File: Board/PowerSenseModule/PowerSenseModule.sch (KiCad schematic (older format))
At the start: 28 parts, among them J1 Conn_01x06_Male, U1 TPS82150

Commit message: Generated gerber and fab files
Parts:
- added G1: LOGO, Logo:HKNZetaChi, symbol F1_Logo:LOGO
- H1, H2, H3, H4: value MountingHole_Pad -> (none)
- J1: value Conn_01x06_Male -> DT13-6P
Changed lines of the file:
@@
 Sheet 1 2
 Title "Power Sense Module - Main Page and Power"
-Date ""
+Date "2019-12-18"
 Rev ""
 Comp "University of Central Florida - HKN Zeta Chi"
@@
 P 1525 3600
 F 0 "J1" H 1633 3981 50  0000 C CNN
-F 1 "Conn_01x06_Male" H 1633 3890 50  0000 C CNN
+F 1 "DT13-6P" H 1633 3890 50  0000 C CNN
 F 2 "Connector_TE:DT13-6P" H 1525 3600 50  0001 C CNN
 F 3 "https://www.te.com/commerce/DocumentDelivery/DDEController?Action=showdoc&DocId=Customer+Drawing%7FDT13-4P%7FC%7Fpdf%7FEnglish%7FENG_CD_DT13-4P_C.pdf%7FDT13-4P" H 1525 3600 50  0001 C CNN
@@
 P 9625 5675
 F 0 "H4" H 9725 5724 50  0000 L CNN
-F 1 "MountingHole_Pad" H 9300 5900 50  0000 L CNN
+F 1 " " H 9300 5900 50  0001 L CNN
 F 2 "MountingHole:MountingHole_2.7mm_M2.5_Pad" H 9625 5675 50  0001 C CNN
 F 3 "~" H 9625 5675 50  0001 C CNN
@@
 P 8500 5675
 F 0 "H2" H 8600 5724 50  0000 L CNN
-F 1 "MountingHole_Pad" H 8175 5900 50  0000 L CNN
+F 1 " " H 8175 5900 50  0001 L CNN
 F 2 "MountingHole:MountingHole_2.7mm_M2.5_Pad" H 8500 5675 50  0001 C CNN
 F 3 "~" H 8500 5675 50  0001 C CNN
@@
 P 9075 5675
 F 0 "H3" H 9175 5724 50  0000 L CNN
-F 1 "MountingHole_Pad" H 8725 6025 50  0000 L CNN
+F 1 " " H 8725 6025 50  0000 L CNN
 F 2 "MountingHole:MountingHole_2.7mm_M2.5_Pad" H 9075 5675 50  0001 C CNN
 F 3 "~" H 9075 5675 50  0001 C CNN
@@
 P 7950 5675
 F 0 "H1" H 8050 5724 50  0000 L CNN
-F 1 "MountingHole_Pad" H 7625 6025 50  0000 L CNN
+F 1 " " H 7625 6025 50  0001 L CNN
 F 2 "MountingHole:MountingHole_2.7mm_M2.5_Pad" H 7950 5675 50  0001 C CNN
 F 3 "~" H 7950 5675 50  0001 C CNN
@@
 Text Notes 3180 5090 0    50   ~ 0
 CAN+ (CANH) and CAN- (CANL) renamed \nto use differential pair KiCAD feature
+$Comp
+L F1_Logo:LOGO G1
+U 1 1 5E08FC59
+P 10855 6840
+F 0 "G1" H 10855 6579 60  0001 C CNN
+F 1 "LOGO" H 10855 7101 60  0001 C CNN
+F 2 "Logo:HKNZetaChi" H 10854 7153 50  0001 C CNN
+F 3 "" H 10855 6840 50  0001 C CNN
+	1    10855 6840
+	1    0    0    -1
+$EndComp
 $EndSCHEMATC

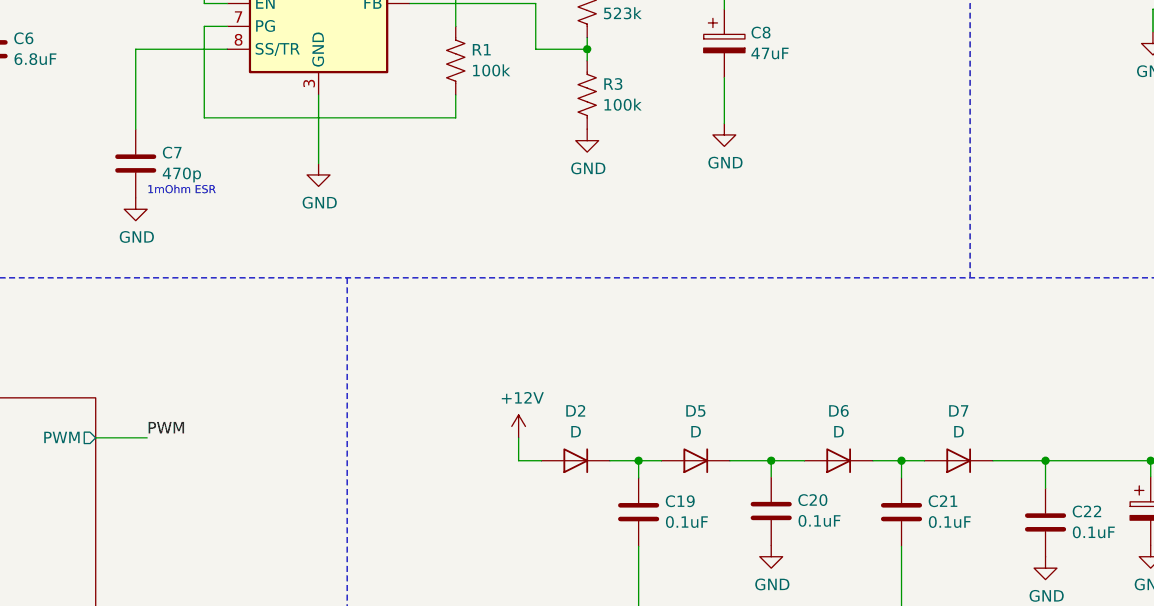
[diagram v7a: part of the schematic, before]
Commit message: Created BOM
BOM was created by adding symbol fields then using the KiCAD BOM Wizard plugin 
https://hackaday.io/project/20765-kicad-bom-wizard
Then the CSV data was imported into Excel and was tweaked.
Price per unit is about $35-40
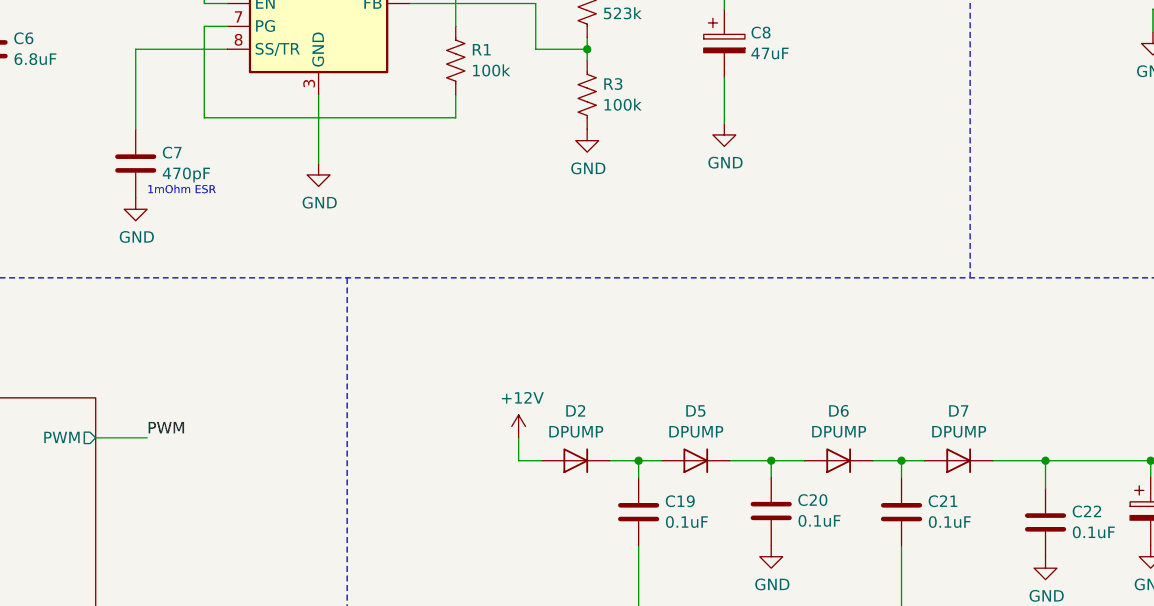
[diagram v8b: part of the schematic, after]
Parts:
- C1: Manufacturer (none) -> KEMET; Manufacturer PN (none) -> C0603X479C1HACTU; Price 1 QTY (none) -> 0.12; Supplier (none) -> Mouser; Supplier Link (none) -> https://www.mouser.com/ProductDetail/KEMET/C0603X479C1HACTU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; Supplier PN (none) -> 80-C0603X479C1HACTU
- C19, C20, C21, C22: footprint Capacitor_SMD:C_0603_1608Metric -> Capacitor_SMD:C_0603_1608Metric_Pad1.05x0.95mm_HandSolder; Manufacturer PN (none) -> CGA3E2X7R1H104K080AA; Price 1 QTY (none) -> 0.1; Supplier (none) -> Mouser; Supplier Link (none) -> https://www.mouser.com/ProductDetail/TDK/CGA3E2X7R1H104K080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; Supplier PN (none) -> 810-CGA3E2X7R1H104K
- C2: Manufacturer (none) -> KEMET; Manufacturer PN (none) -> C0603C471J5GAC7411; Price 1 QTY (none) -> 0.21; Supplier (none) -> Mouser; Supplier Link (none) -> https://www.mouser.com/ProductDetail/KEMET/C0603C471J5GAC74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; Supplier PN (none) -> -C0603C471J5G7411
- C23: footprint Capacitor_SMD:CP_Elec_4x5.8 -> Capacitor_SMD:C_0805_2012Metric_Pad1.15x1.40mm_HandSolder; Manufacturer (none) -> TDK; Manufacturer PN (none) -> CGA4J1X7R1H475K125AC; Price 1 QTY (none) -> 0.69; Supplier (none) -> Mouser; Supplier Link (none) -> https://www.mouser.com/ProductDetail/TDK/CGA4J1X7R1H475K125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; Supplier PN (none) -> 810-CGA4J1X7R1H475K1
- C3: Manufacturer (none) -> KEMET; Manufacturer PN (none) -> C0603C103J5RACTU; Price 1 QTY (none) -> 0.10; Supplier (none) -> Mouser; Supplier Link (none) -> https://www.mouser.com/ProductDetail/KEMET/C0603C103J5RACTU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; Supplier PN (none) -> 80-C0603C103J5R
- C4: Manufacturer (none) -> TDK; Manufacturer PN (none) -> CGA3E2X7R1H104K080AA; Price 1 QTY (none) -> 0.1; Supplier (none) -> Mouser; Supplier Link (none) -> https://www.mouser.com/ProductDetail/TDK/CGA3E2X7R1H104K080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; Supplier PN (none) -> 810-CGA3E2X7R1H104K
- C5: footprint Capacitor_SMD:C_0603_1608Metric_Pad1.05x0.95mm_HandSolder -> Capacitor_SMD:C_0805_2012Metric_Pad1.15x1.40mm_HandSolder; Manufacturer (none) -> TDK; Manufacturer PN (none) -> CGA4J1X7R1H475K125AC; Price 1 QTY (none) -> 0.69; Supplier (none) -> Mouser; Supplier Link (none) -> https://www.mouser.com/ProductDetail/TDK/CGA4J1X7R1H475K125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; Supplier PN (none) -> 810-CGA4J1X7R1H475K1
- C6: Manufacturer (none) -> TDK; Manufacturer PN (none) -> CGA5L1X7R1V685K160AC; Price 1 QTY (none) -> 0.97; Supplier (none) -> Mouser; Supplier Link (none) -> https://www.mouser.com/ProductDetail/TDK/CGA5L1X7R1V685K160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; Supplier PN (none) -> 810-CGA5L1X7R1V685KC
- C7: value 470p -> 470pF; Manufacturer (none) -> KEMET; Manufacturer PN (none) -> C0603C471J5GAC7411; Price 1 QTY (none) -> 0.21; Supplier (none) -> Mouser; Supplier Link (none) -> https://www.mouser.com/ProductDetail/KEMET/C0603C471J5GAC74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; Supplier PN (none) -> -C0603C471J5G7411
- C8: Manufacturer (none) -> Panasonic; Manufacturer PN (none) -> EEE-FT1C470AR; Price 1 QTY (none) -> 0.42; Supplier (none) -> Mouser; Supplier Link (none) -> https://www.mouser.com/ProductDetail/Panasonic/EEE-FT1C470A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; Supplier PN (none) -> 667-EEE-FT1C470AR
- D1: Supplier Link (none) -> https://www.mouser.com/ProductDetail/Diodes-Incorporated/SD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
- D2, D5, D6, D7: value D -> DPUMP
- J1: Manufacturer (none) -> TE Connectivity / DEUTSCH; Manufacturer PN (none) -> DT13-6P; Price 1 QTY (none) -> 9.15; Supplier (none) -> Mouser; Supplier Link (none) -> https://www.mouser.com/ProductDetail/TE-Connectivity-DEUTSC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; Supplier PN (none) -> 571-DT13-6P
- R1, R3: Manufacturer (none) -> Vishay / Dale; Manufacturer PN (none) -> CRCW0603100KFKEA; Price 1 QTY (none) -> 0.1; Supplier (none) -> Mouser; Supplier Link (none) -> https://www.mouser.com/ProductDetail/Vishay-Dale/CRCW060310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; Supplier PN (none) -> 71-CRCW0603-100K-E3
- R2: Manufacturer (none) -> Bourns; Manufacturer PN (none) -> CR0603-FX-5233ELF; Price 1 QTY (none) -> 0.1; Supplier (none) -> Mouser; Supplier Link (none) -> https://www.mouser.com/ProductDetail/Bourns/CR0603-FX-5233E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; Supplier PN (none) -> 652-CR0603FX-5233ELF
